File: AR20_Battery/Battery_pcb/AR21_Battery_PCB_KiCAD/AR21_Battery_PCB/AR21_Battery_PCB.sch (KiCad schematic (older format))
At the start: 4 parts, among them J1 Conn_01x01_Female, J2 Conn_01x01_Male, J3 Conn_01x01_Male, J4 Conn_01x01_Female

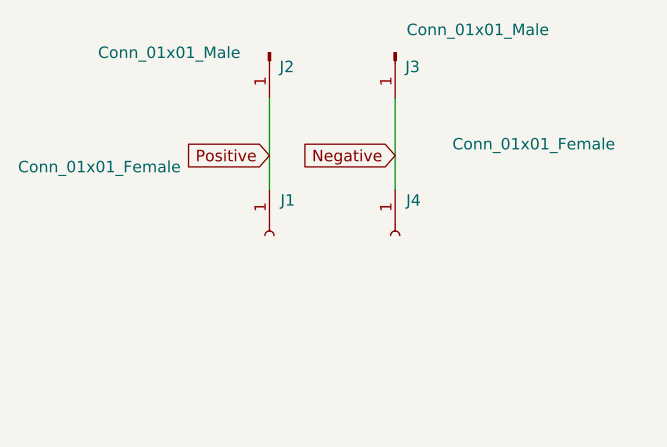
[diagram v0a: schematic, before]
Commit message: Fixed: Mounting holes
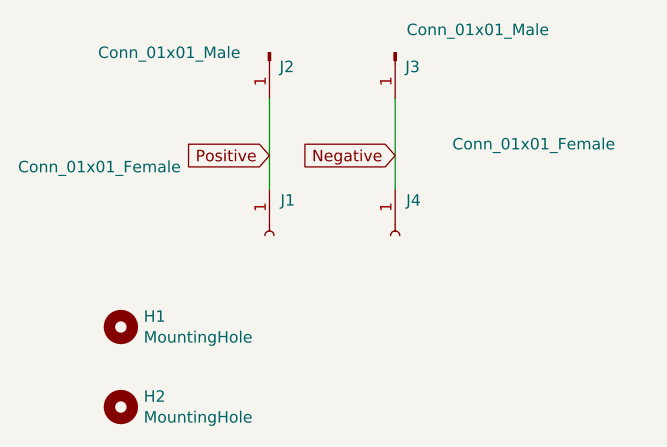
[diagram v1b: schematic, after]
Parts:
- added H1, H2: MountingHole, AR21_Battery_lib:M3 hole, symbol Mechanical:MountingHole
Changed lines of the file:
@@
 Text GLabel 3550 3150 0    50   Input ~ 0
 Negative
+$Comp
+L Mechanical:MountingHole H1
+U 1 1 5FD6F3F5
+P 2350 3900
+F 0 "H1" H 2450 3946 50  0000 L CNN
+F 1 "MountingHole" H 2450 3855 50  0000 L CNN
+F 2 "AR21_Battery_lib:M3 hole" H 2350 3900 50  0001 C CNN
+F 3 "~" H 2350 3900 50  0001 C CNN
+	1    2350 3900
+	1    0    0    -1
+$EndComp
+$Comp
+L Mechanical:MountingHole H2
+U 1 1 5FD6FC07
+P 2350 4250
+F 0 "H2" H 2450 4296 50  0000 L CNN
+F 1 "MountingHole" H 2450 4205 50  0000 L CNN
+F 2 "AR21_Battery_lib:M3 hole" H 2350 4250 50  0001 C CNN
+F 3 "~" H 2350 4250 50  0001 C CNN
+	1    2350 4250
+	1    0    0    -1
+$EndComp
 $EndSCHEMATC
